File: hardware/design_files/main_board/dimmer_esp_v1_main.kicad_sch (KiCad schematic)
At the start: 54 parts, among them IC1 PEC11S-929K-S0015, J1 Screw_Terminal_01x03, J2 SM05B-SRSS-TB_LF__SN_, J3 Conn_01x02, K1 FTR-LYCA005Y, Q1 BC817, SW1 Commission, SW2 Toggle, SW3 Reset, U1 SGM2212-3.3XKC3G/TR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

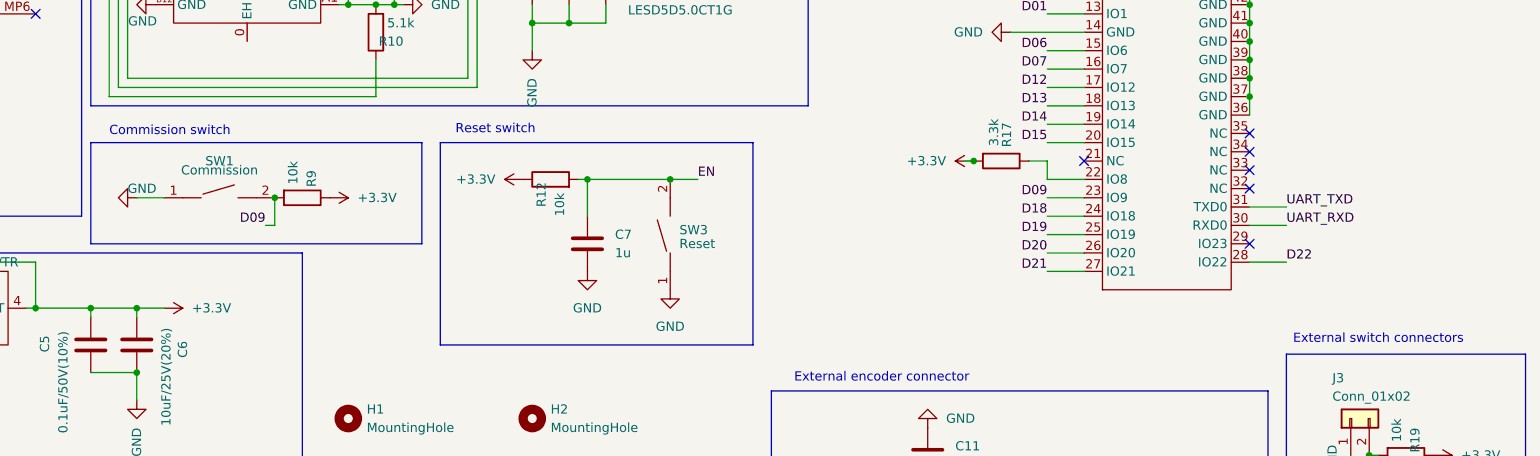
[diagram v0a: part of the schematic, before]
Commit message: Hardware: Switch button pin from GPIO09 (strapping pin) to GPIO23
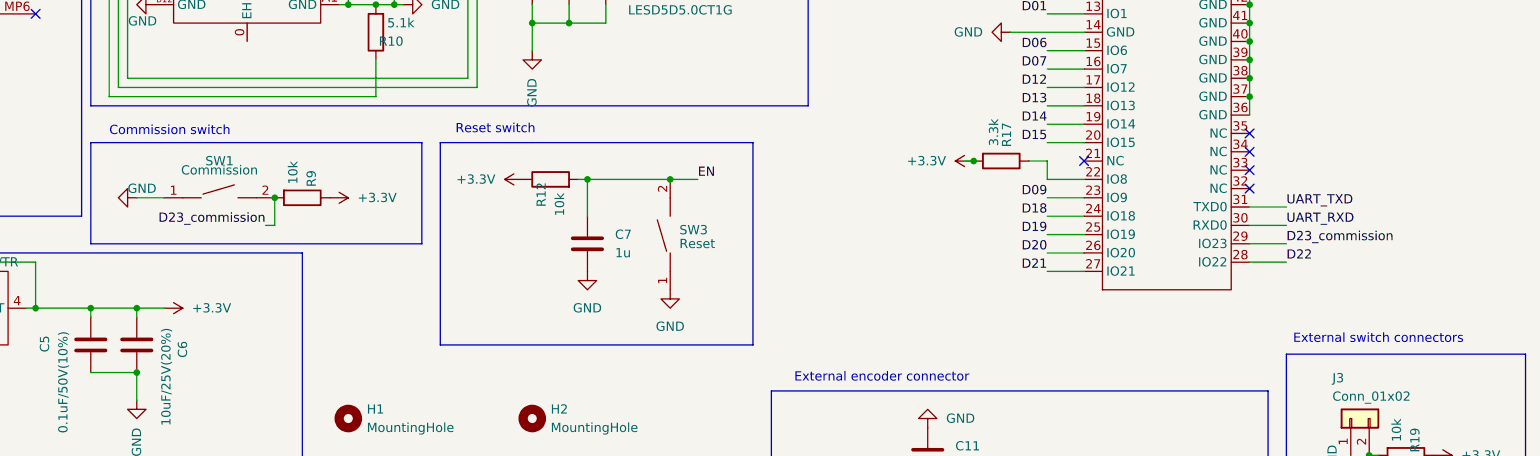
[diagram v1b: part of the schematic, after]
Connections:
- net D09: no longer R9.2, SW1.2
- net D23_commission: now reaches U4.29 (IO23)
- net D23_commission: now also R9.2, SW1.2
- no-connect marks 25 -> 24
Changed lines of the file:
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@@
-	)
-	(no_connect
-		(at 246.38 87.63)
 	)
 	(no_connect
@@
 	(wire
 		(pts
+			(xy 246.38 87.63) (xy 251.46 87.63)
+		)
+		(stroke
+			(width 0)
+			(type default)
+		)
+	)
+	(wire
+		(pts
 			(xy 44.45 45.72) (xy 50.8 45.72)
 		)
@@
 		)
 	)
-	(label "D09"
-		(at 110.49 85.09 180)
-		(effects
-			(font
-				(size 1.27 1.27)
-			)
-			(justify right bottom)
-		)
-	)
 	(label "D06"
 		(at 218.44 60.96 180)
@@
 		)
 	)
+	(label "D23_commission"
+		(at 110.49 85.09 180)
+		(effects
+			(font
+				(size 1.27 1.27)
+			)
+			(justify right bottom)
+		)
+	)
 	(label "HV1"
 		(at 45.72 132.08 0)
@@
 		)
 	)
+	(label "D23_commission"
+		(at 251.46 87.63 0)
+		(effects
+			(font
+				(size 1.27 1.27)
+			)
+			(justify left bottom)
+		)
+	)

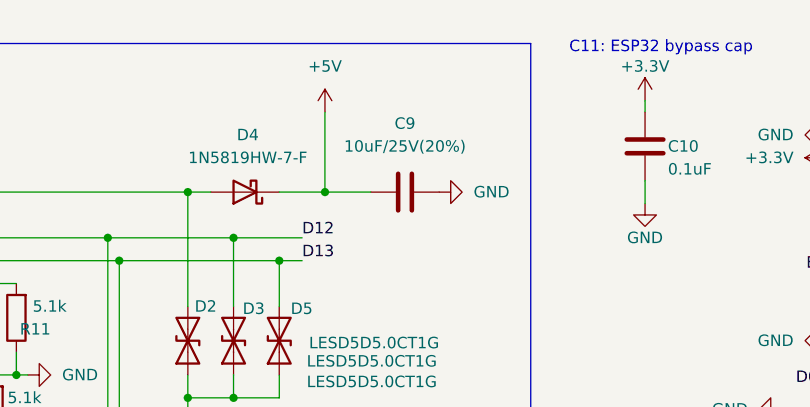
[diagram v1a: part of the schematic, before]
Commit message: Hardware: Rename C9 back to C8, fix tracks
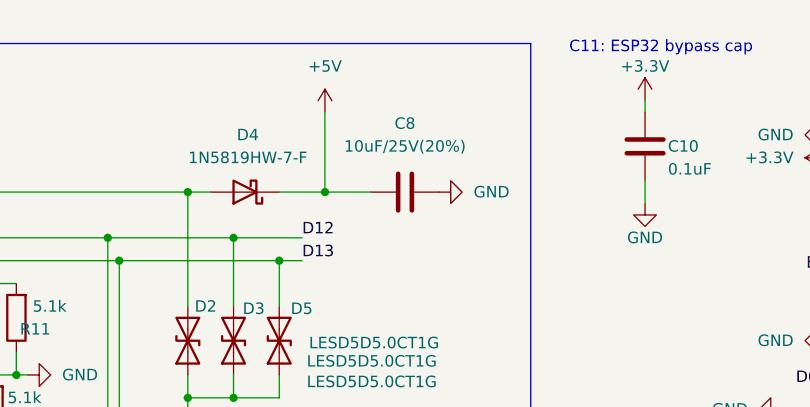
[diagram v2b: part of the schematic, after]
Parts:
- renumbered C9 to C8
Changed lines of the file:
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@@
 		(dnp no)
 		(fields_autoplaced yes)
-		(property "Reference" "C9"
+		(property "Reference" "C8"
 			(at 171.45 26.67 90)
 			(show_name no)
@@
 			(project "dimmer_esp_v1_main"
 				(path "/ddfcd425-273c-4c73-9404-db5c5faab60e"
-					(reference "C9")
+					(reference "C8")
 					(unit 1)
 				)

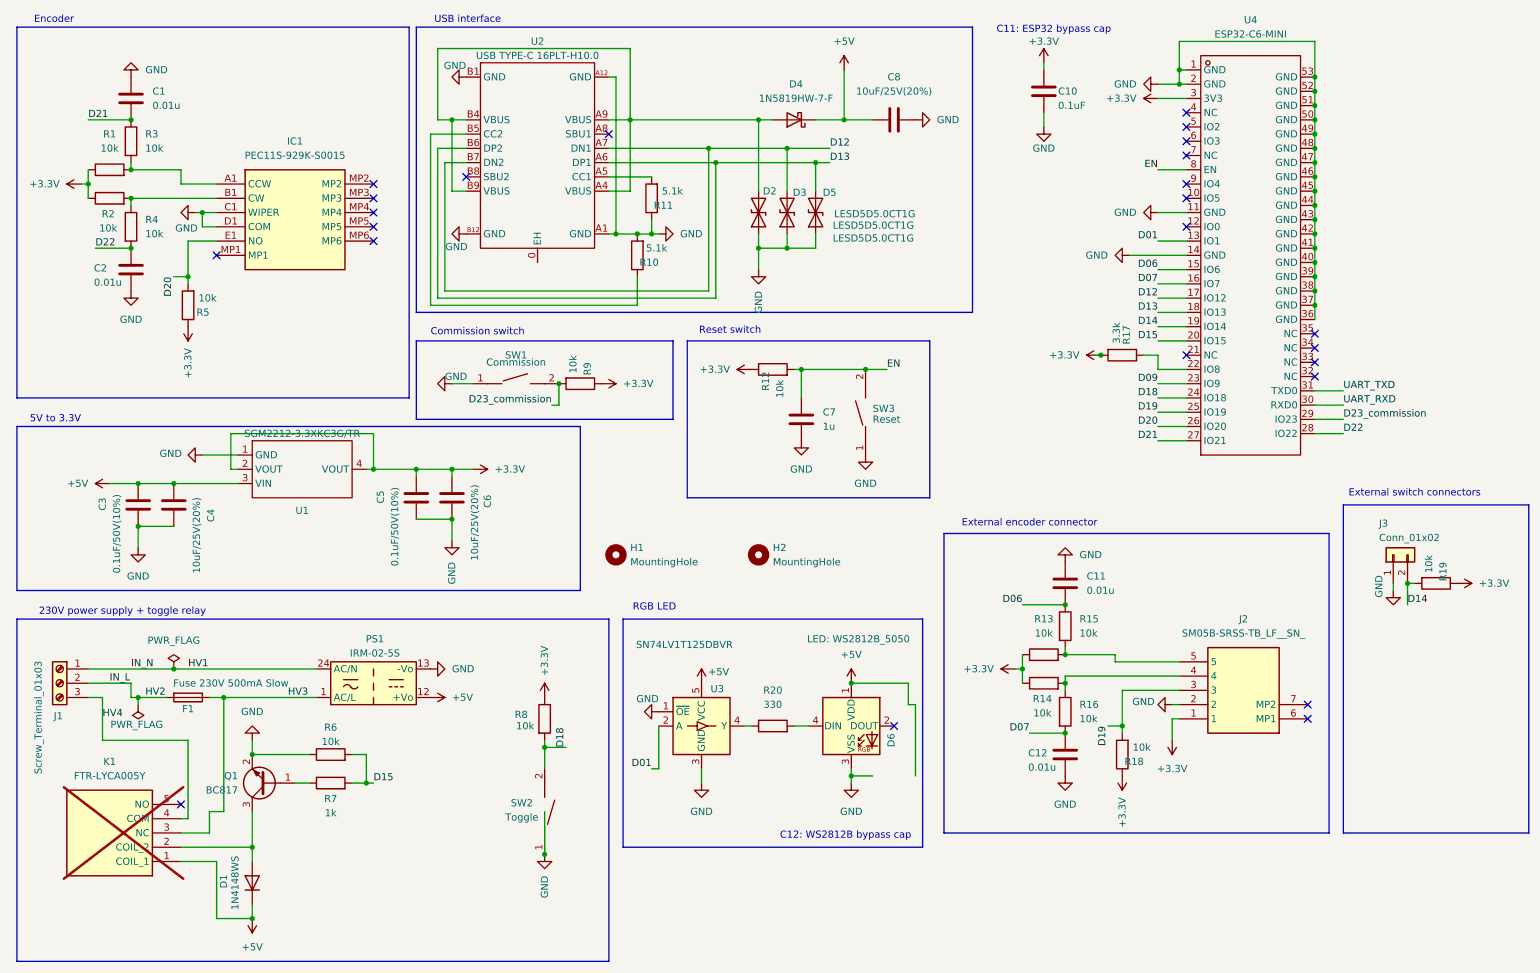
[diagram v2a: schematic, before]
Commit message: Hardware: Switch relay pin from D15 (strapping pin) to D02
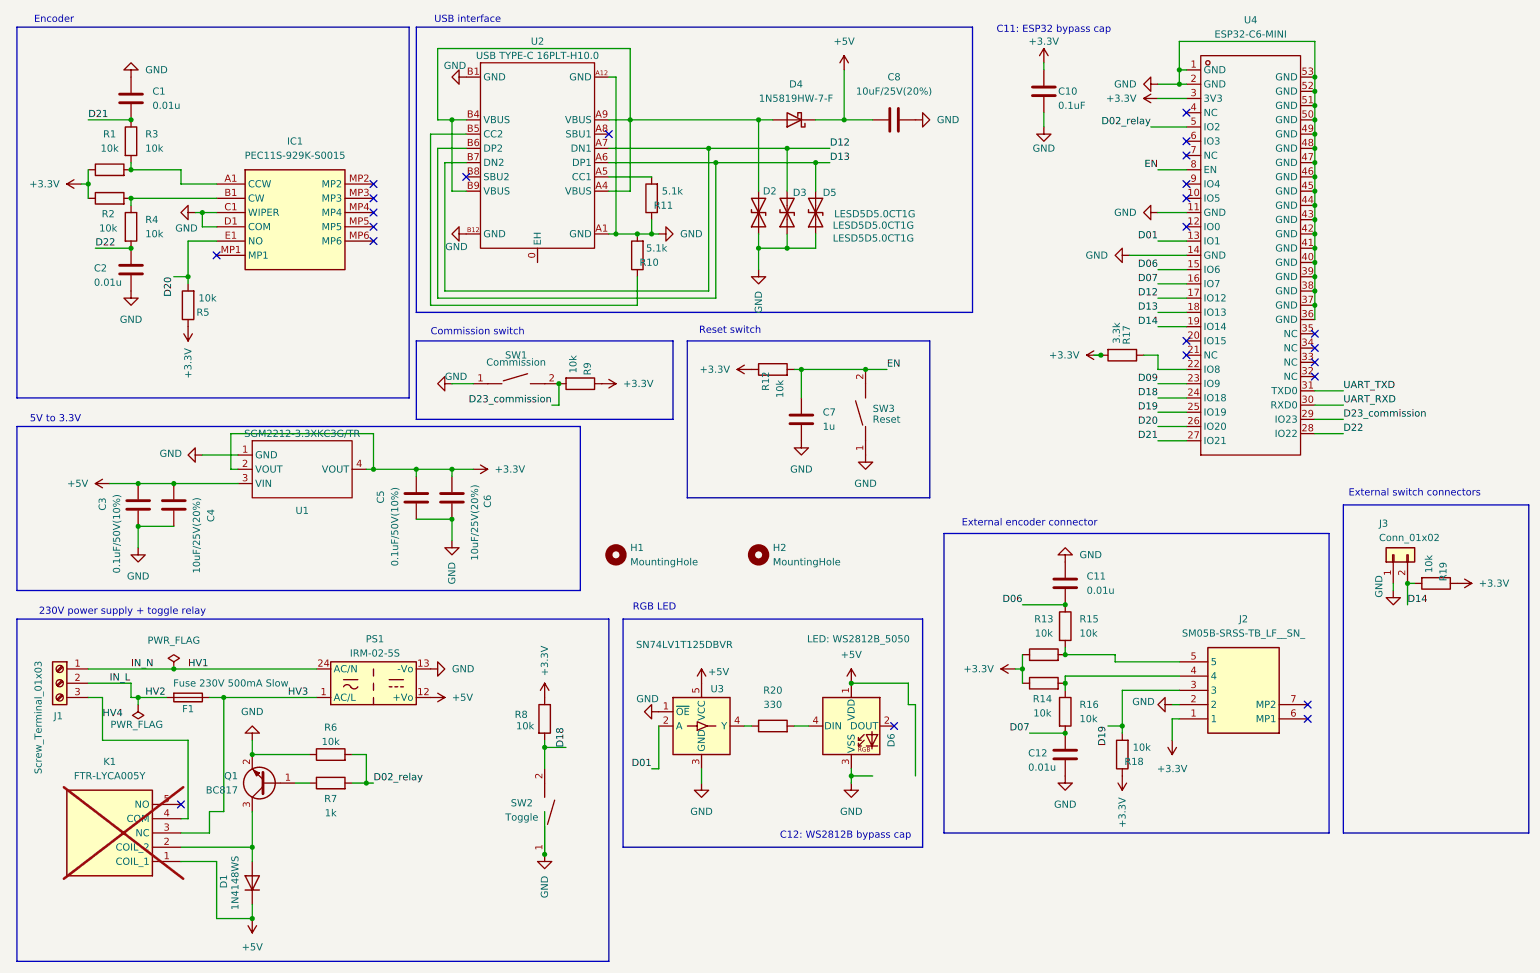
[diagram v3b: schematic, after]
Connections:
- net D02_relay: now reaches U4.5 (IO2)
- net D02_relay: now also R6.2, R7.2
- removed net D15: R6.2, R7.2, U4.20 (IO15)
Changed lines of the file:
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@@
+	)
+	(no_connect
+		(at 223.52 73.66)
 	)
 	(no_connect
@@
 	)
 	(no_connect
-		(at 223.52 35.56)
-	)
-	(no_connect
 		(at 223.52 38.1)
 	)
@@
 	(wire
 		(pts
+			(xy 217.17 35.56) (xy 223.52 35.56)
+		)
+		(stroke
+			(width 0)
+			(type default)
+		)
+	)
+	(wire
+		(pts
 			(xy 53.34 90.17) (xy 78.74 90.17)
 		)
@@
 		(pts
 			(xy 173.99 138.43) (xy 173.99 134.62)
-		)
-		(stroke
-			(width 0)
-			(type default)
-		)
-	)
-	(wire
-		(pts
-			(xy 218.44 73.66) (xy 223.52 73.66)
 		)
 		(stroke
@@
 		)
 	)
+	(label "D02_relay"
+		(at 78.74 152.4 0)
+		(effects
+			(font
+				(size 1.27 1.27)
+			)
+			(justify left bottom)
+		)
+	)
 	(label "D18"
 		(at 218.44 83.82 180)
@@
 		)
 	)
-	(label "D15"
-		(at 78.74 152.4 0)
-		(effects
-			(font
-				(size 1.27 1.27)
-			)
-			(justify left bottom)
-		)
-	)
 	(label "UART_TXD"
 		(at 251.46 82.55 0)
@@
 		)
 	)
+	(label "D02_relay"
+		(at 217.17 35.56 180)
+		(effects
+			(font
+				(size 1.27 1.27)
+			)
+			(justify right bottom)
+		)
+	)
 	(label "HV1"
 		(at 45.72 132.08 0)
@@
 		)
 	)
-	(label "D15"
-		(at 218.44 73.66 180)
-		(effects
-			(font
-				(size 1.27 1.27)
-			)
-			(justify right bottom)
-		)
-	)
